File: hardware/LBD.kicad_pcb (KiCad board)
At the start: 2 copper layers, 13.4 x 46.9 mm, 10 parts, among them J2 USB4155-03-C_REVA, U1 RP2040, U4 TPSM828214SILR

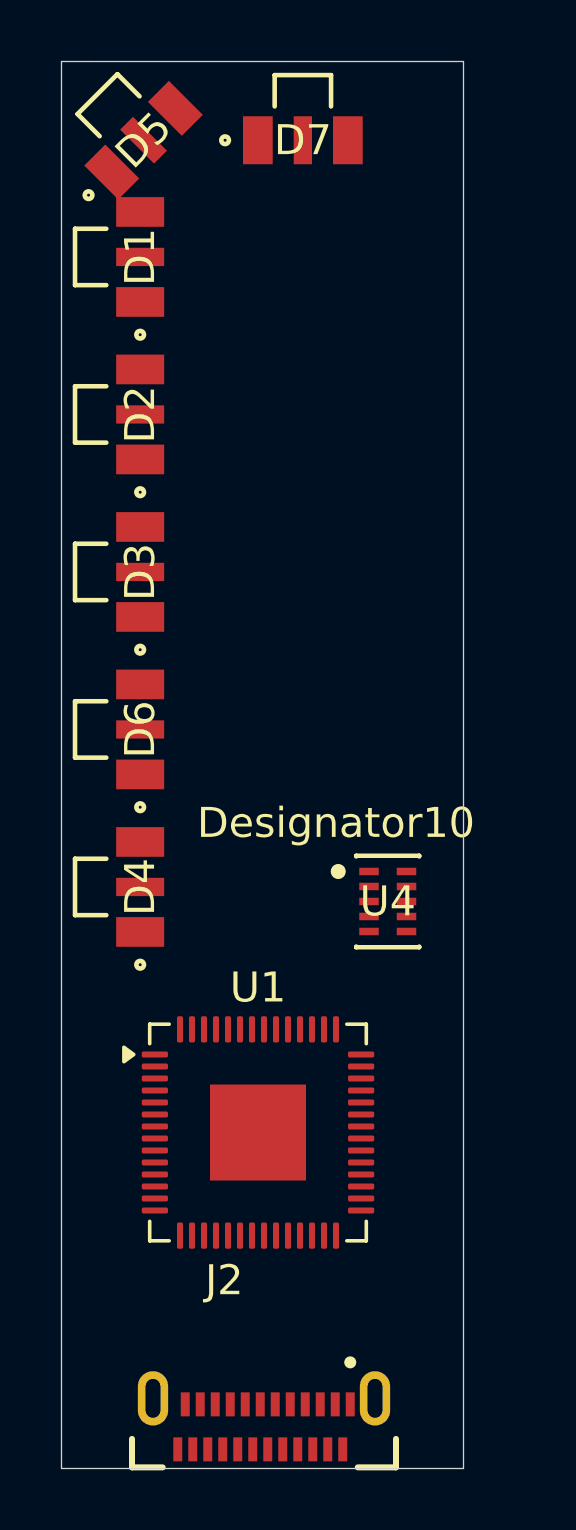
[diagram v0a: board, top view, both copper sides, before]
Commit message: resositioned leds
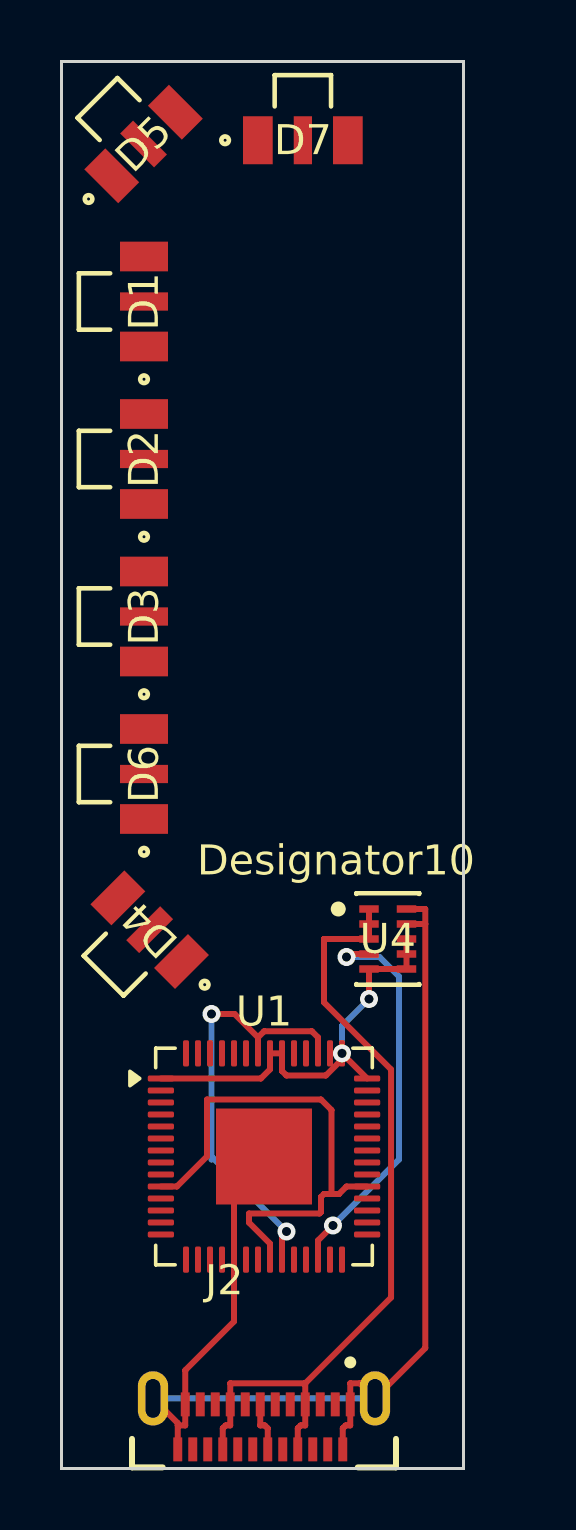
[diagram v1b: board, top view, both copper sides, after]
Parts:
- moved D1 1.49 mm to (143.0, 86.5)
- moved D2 1.49 mm to (143.0, 91.8)
- moved D3 1.49 mm to (143.0, 97.0)
- moved D6 1.49 mm to (143.0, 102.2)
- moved D4 1.46 mm to (143.2, 107.4), turned to 135 degrees
- moved U4 1.25 mm to (151.1, 107.8)
- moved U1 0.82 mm to (147.0, 115.0)
- moved D5 0.13 mm to (143.0, 81.2)
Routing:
- net GND: track 0.00 -> 41.4 mm
- net +3.3V: track 0.00 -> 32.2 mm, vias 0 -> 2
- net VBUS: track 0.00 -> 26.7 mm
- net +1V1: track 0.00 -> 14.5 mm, vias 0 -> 2
- net /Power/PG: track 0.00 -> 13.4 mm, vias 0 -> 2
- net /USB/DN: track 0.00 -> 1.69 mm
